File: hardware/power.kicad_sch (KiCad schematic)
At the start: 8 parts, among them U4 MD57E33QA3, U5 MD57E33QA3, U7 TP4054

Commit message: battery switching
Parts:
- added C28: 1uF, Capacitor_SMD:C_0805_2012Metric_Pad1.18x1.45mm_HandSolder, symbol Device:C
- added D1: 1N5819WS, Diode_SMD:D_SOD-323, symbol Diode:1N5819WS
- added D2: LED, symbol Device:LED
- added Q1: AO3401A, Package_TO_SOT_SMD:SOT-23, symbol Transistor_FET:AO3401A
- added R7: 100k, Resistor_SMD:R_0805_2012Metric_Pad1.20x1.40mm_HandSolder, symbol Device:R
- added R8, R9: 2k, Resistor_SMD:R_0805_2012Metric_Pad1.20x1.40mm_HandSolder, symbol Device:R
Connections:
- net +5V: now also C28.1, D1.1 (K), Q1.3 (D)
- net +BATT: now also Q1.2 (S)
- net GND: now also C28.2, R7.2, R8.2
- net VBUS: now also D1.2 (A), Q1.1 (G), R7.1, R9.1
- net at U7.1 (~{CHRG}): now also D2.1 (K)
- net at U7.5 (PROG): now also R8.1
- new net: D2.2 (A), R9.2

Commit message: layout + some routing
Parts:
- added J4: JST PH S2B, Connector_JST:JST_PH_S2B-PH-SM4-TB_1x02-1MP_P2.00mm_Horizontal, symbol Connector_Generic_MountingPin:Conn_01x02_MountingPin
- added SW8: SW_SPDT, Button_Switch_SMD:SW_SPDT_PCM12, symbol Switch:SW_SPDT
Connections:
- net +5V: now also SW8.2 (B); no longer C28.1, D1.1 (K), Q1.3 (D)
- net +BATT: now also J4.1 (Pin_1)
- net GND: now also J4.2 (Pin_2)
- new net: C28.1, D1.1 (K), Q1.3 (D), SW8.3 (C)

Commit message: feat: routing
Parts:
- D2: footprint (none) -> LED_SMD:LED_0805_2012Metric
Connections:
- net at C28.1, D1.1 (K), Q1.3 (D): now also SW8.1 (A); no longer SW8.3 (C)
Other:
- moved on the sheet: SW8
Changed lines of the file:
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@@
-	(wire
-		(pts
-			(xy 130.81 118.11) (xy 132.08 118.11)
-		)
-		(stroke
-			(width 0)
-			(type default)
-		)
-	)
 	(wire
 		(pts
@@
 	(wire
 		(pts
-			(xy 130.81 109.22) (xy 130.81 118.11)
-		)
-		(stroke
-			(width 0)
-			(type default)
-		)
-	)
-	(wire
-		(pts
 			(xy 160.02 36.83) (xy 160.02 39.37)
 		)
@@
 	(wire
 		(pts
-			(xy 132.08 118.11) (xy 132.08 125.73)
+			(xy 130.81 109.22) (xy 130.81 130.81)
 		)
 		(stroke
@@
 		(pts
 			(xy 57.15 54.61) (xy 67.31 54.61)
+		)
+		(stroke
+			(width 0)
+			(type default)
+		)
+	)
+	(wire
+		(pts
+			(xy 130.81 130.81) (xy 132.08 130.81)
 		)
 		(stroke
@@
 			)
 		)
-		(property "Footprint" ""
+		(property "Footprint" "LED_SMD:LED_0805_2012Metric"
 			(at 132.08 40.64 0)
 			(effects
@@
 	(symbol
 		(lib_id "Switch:SW_SPDT")
-		(at 137.16 125.73 0)
+		(at 137.16 130.81 0)
 		(unit 1)
 		(exclude_from_sim no)
@@
 		(fields_autoplaced yes)
 		(property "Reference" "SW8"
-			(at 137.16 117.9025 0)
+			(at 137.16 122.9825 0)
 			(effects
 				(font
@@
 		)
 		(property "Value" "SW_SPDT"
-			(at 137.16 120.3268 0)
+			(at 137.16 125.4068 0)
 			(effects
 				(font
@@
 		)
 		(property "Footprint" "Button_Switch_SMD:SW_SPDT_PCM12"
-			(at 137.16 125.73 0)
+			(at 137.16 130.81 0)
 			(effects
 				(font
@@
 		)
 		(property "Datasheet" "~"
-			(at 137.16 133.35 0)
+			(at 137.16 138.43 0)
 			(effects
 				(font
@@
 		)
 		(property "Description" "Switch, single pole double throw"
-			(at 137.16 125.73 0)
-			(effects
-				(font
+			(at 137.16 130.81 0)
+			(effects
+				(font

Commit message: feat: hfsdr rough
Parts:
- removed SW8: SW_SPDT, Button_Switch_SMD:SW_SPDT_PCM12, symbol Switch:SW_SPDT
- added SW3: MST-22D18G4-WT, easyeda2kicad:SW-SMD_MST-22D18G4-WT, symbol easyeda2kicad:MST-22D18G4-WT
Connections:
- net +5V: now also SW3.2
- net at C28.1, D1.1 (K), Q1.3 (D): now also SW3.3
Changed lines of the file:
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@@
-	(wire
-		(pts
-			(xy 142.24 128.27) (xy 162.56 128.27)
-		)
-		(stroke
-			(width 0)
-			(type default)
-		)
-	)
 	(wire
 		(pts
@@
 	(wire
 		(pts
+			(xy 135.89 130.81) (xy 135.89 128.27)
+		)
+		(stroke
+			(width 0)
+			(type default)
+		)
+	)
+	(wire
+		(pts
 			(xy 181.61 57.15) (xy 160.02 57.15)
 		)
@@
 	(wire
 		(pts
+			(xy 135.89 128.27) (xy 162.56 128.27)
+		)
+		(stroke
+			(width 0)
+			(type default)
+		)
+	)
+	(wire
+		(pts
 			(xy 181.61 54.61) (xy 181.61 57.15)
 		)
@@
 		(pts
 			(xy 57.15 54.61) (xy 67.31 54.61)
-		)
-		(stroke
-			(width 0)
-			(type default)
-		)
-	)
-	(wire
-		(pts
-			(xy 130.81 130.81) (xy 132.08 130.81)
 		)
 		(stroke
@@
 	)
 	(symbol
-		(lib_id "Switch:SW_SPDT")
-		(at 137.16 130.81 0)
-		(unit 1)
-		(exclude_from_sim no)
-		(in_bom yes)
-		(on_board yes)
-		(dnp no)
-		(fields_autoplaced yes)
-		(property "Reference" "SW8"
-			(at 137.16 122.9825 0)
-			(effects
-				(font
-					(size 1.27 1.27)
-				)
-			)
-		)
-		(property "Value" "SW_SPDT"
-			(at 137.16 125.4068 0)
-			(effects
-				(font
-					(size 1.27 1.27)
-				)
-			)
-		)
-		(property "Footprint" "Button_Switch_SMD:SW_SPDT_PCM12"
-			(at 137.16 130.81 0)
-			(effects
-				(font
-					(size 1.27 1.27)
-				)
-				(hide yes)
-			)
-		)
-		(property "Datasheet" "~"
-			(at 137.16 138.43 0)
-			(effects
-				(font
-					(size 1.27 1.27)
-				)
-				(hide yes)
-			)
-		)
-		(property "Description" "Switch, single pole double throw"
-			(at 137.16 130.81 0)
-			(effects
-				(font
-					(size 1.27 1.27)
-				)
-				(hide yes)
-			)
-		)
-		(pin "2"
-		)
-		(pin "1"
-		)
-		(pin "3"
-		)
-		(instances
-			(project "hfsdr"
-				(path "/a11445ed-c3bd-4d1c-a039-1c09b0dceab8/34aaad8d-c78a-4b16-bc41-13b9a7defd8e"
-					(reference "SW8")
-					(unit 1)
-				)
-			)
-		)
-	)
-	(symbol
 		(lib_id "Connector_Generic_MountingPin:Conn_01x02_MountingPin")
 		(at 207.01 120.65 0)
@@
 					(unit 1)
 				)
+			)
+		)
+	)
+	(symbol
+		(lib_id "easyeda2kicad:MST-22D18G4-WT")
+		(at 130.81 135.89 0)
+		(mirror x)
+		(unit 1)
+		(exclude_from_sim no)
+		(in_bom yes)
+		(on_board yes)
+		(dnp no)
+		(property "Reference" "SW3"
+			(at 123.19 135.8899 0)
+			(effects
+				(font
+					(size 1.27 1.27)
+				)
+				(justify right)
+			)
+		)
+		(property "Value" "MST-22D18G4-WT"
+			(at 123.19 138.4299 0)
+			(effects
+				(font
+					(size 1.27 1.27)
+				)
+				(justify right)
+			)
+		)
+		(property "Footprint" "easyeda2kicad:SW-SMD_MST-22D18G4-WT"
+			(at 130.81 123.19 0)
+			(effects
+				(font
+					(size 1.27 1.27)
+				)
+				(hide yes)
+			)
+		)
+		(property "Datasheet" ""
+			(at 130.81 135.89 0)
+			(effects
+				(font
+					(size 1.27 1.27)
+				)
+				(hide yes)
+			)
+		)
+		(property "Description" ""
+			(at 130.81 135.89 0)
+			(effects
+				(font
+					(size 1.27 1.27)
+				)
+				(hide yes)
+			)
+		)
+		(property "LCSC Part" "C7507448"
+			(at 130.81 120.65 0)
+			(effects
+				(font
+					(size 1.27 1.27)
+				)
+				(hide yes)
+			)
+		)
+		(pin "1"
+		)
+		(pin "6"
+		)
+		(pin "4"
+		)
+		(pin "3"
+		)
+		(pin "2"
+		)
+		(pin "5"
+		)
+		(instances
+			(project ""
+				(path "/a11445ed-c3bd-4d1c-a039-1c09b0dceab8/34aaad8d-c78a-4b16-bc41-13b9a7defd8e"
+					(reference "SW3")
+					(unit 1)
+				)

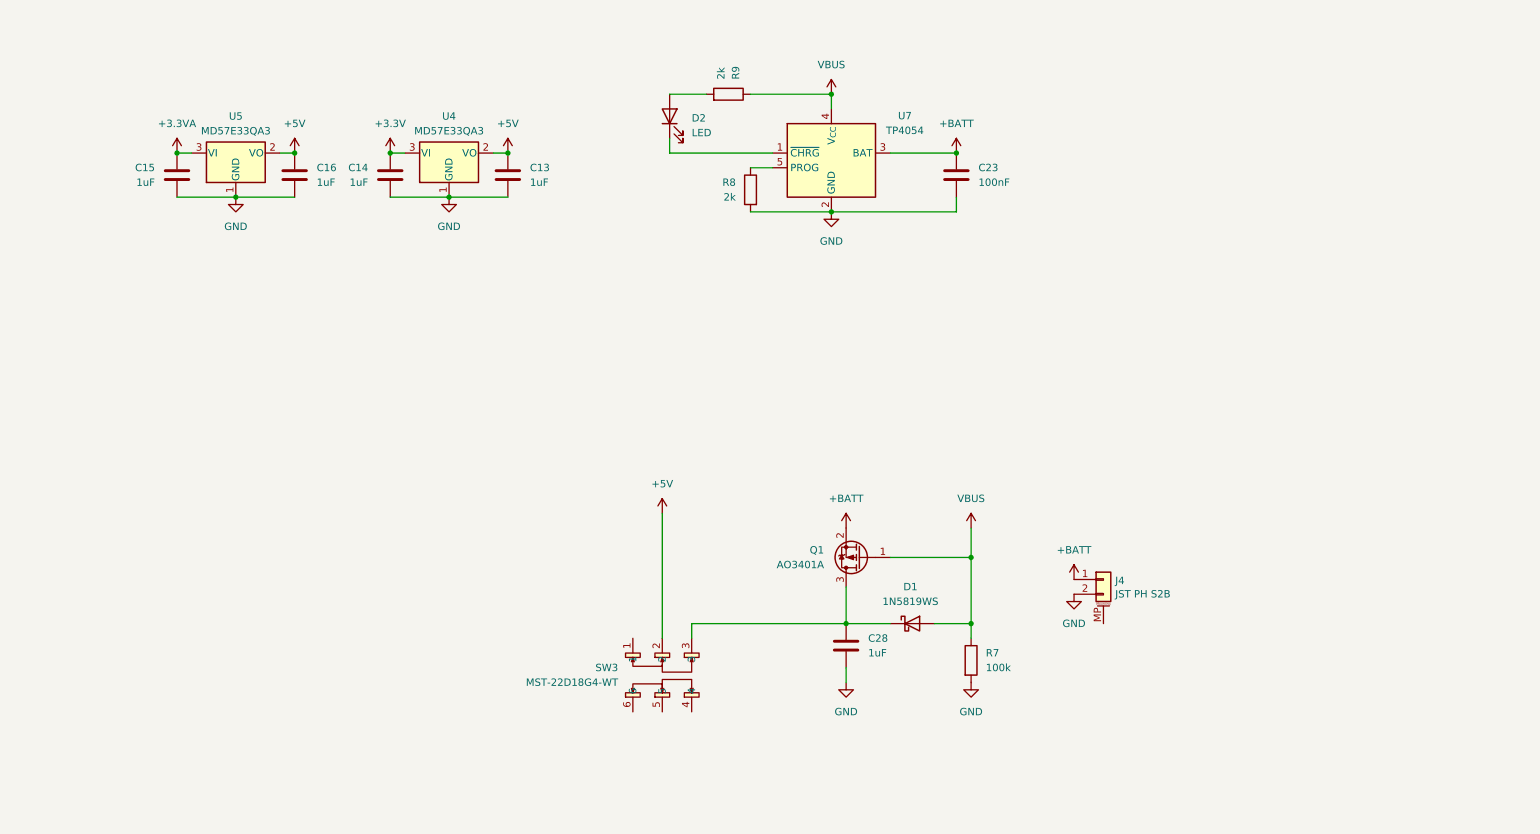
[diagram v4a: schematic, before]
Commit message: feat: add pads + fix adc chip footprint
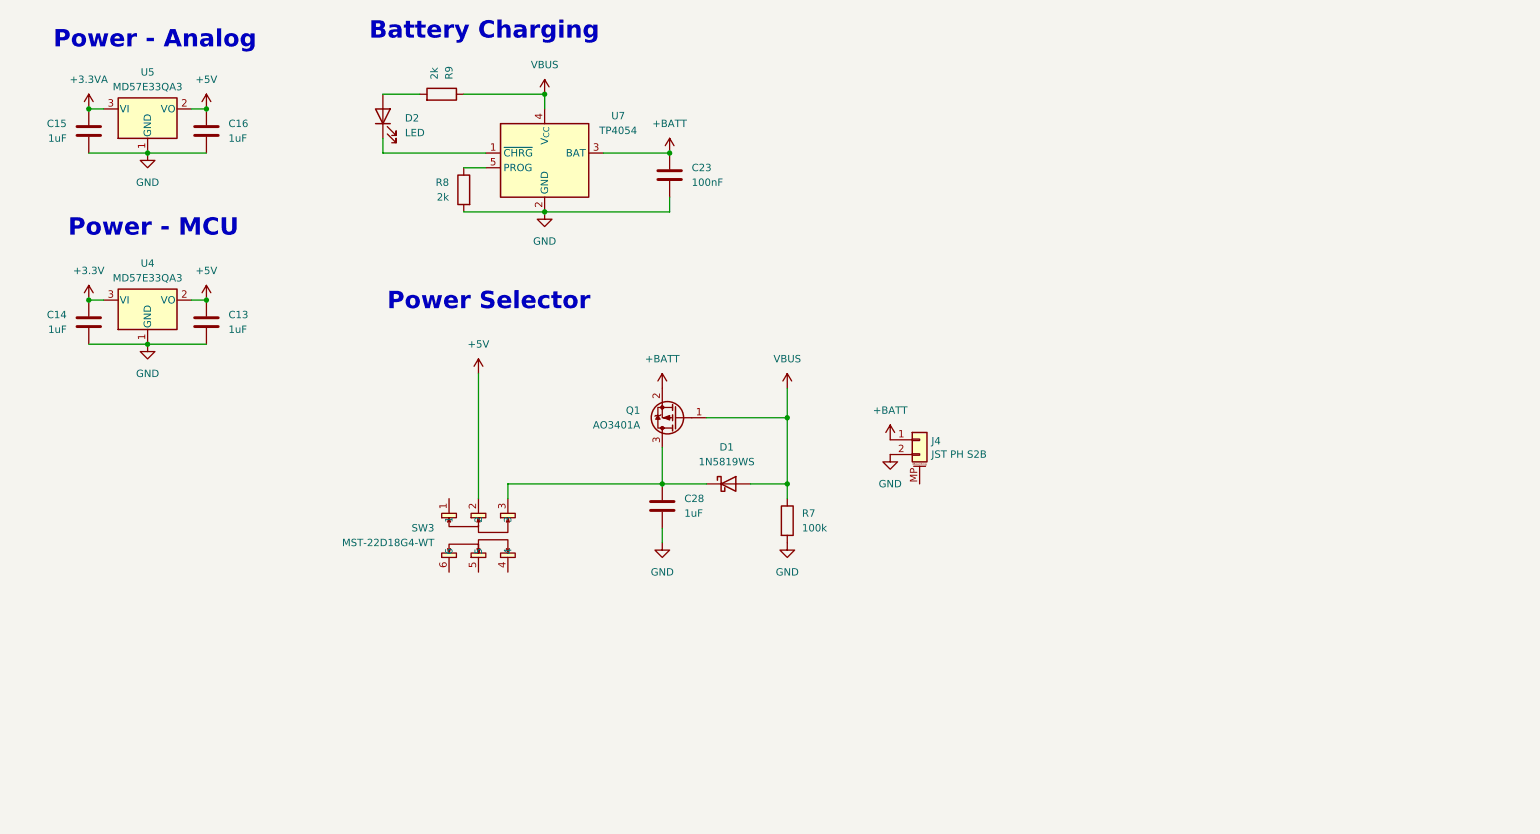
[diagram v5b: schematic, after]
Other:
- note added: "Battery Charging"
- note added: "Power - Analog"
- note added: "Power - MCU"
- note added: "Power Selector"
- moved on the sheet: C13, C14, C15, C16, C23, C28, D1, D2, J4, Q1, R7, R8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

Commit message: Production ready
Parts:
- removed U4, U5: MD57E33QA3, Package_TO_SOT_SMD:SOT-23, symbol Regulator_Linear:TPS7A0520PDBZ
- added R19, R20, R21, R22: 220k, Resistor_SMD:R_0805_2012Metric_Pad1.20x1.40mm_HandSolder, symbol Device:R
- added U10, U9: LMV321, Package_TO_SOT_SMD:SOT-353_SC-70-5, symbol Amplifier_Operational:LMV321
- added U4, U5: MD57E33QC3, easyeda:SOT-23-5_L3.0-W1.7-P0.95-LS2.8-BR, symbol easyeda:MD57E33QC3
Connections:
- net +3.3V: now also U10.5 (V+), U4.5 (VOUT), U9.5 (V+)
- net +3.3VA: now also U5.5 (VOUT)
- net +5V: now also U4.1 (VIN), U4.3 (EN), U5.1 (VIN), U5.3 (EN)
- net +BATT: now also R19.1
- net GND: now also R20.2, R22.2, U10.2 (V-), U4.2 (GND), U5.2 (GND), U9.2 (V-)
- net VBUS: now also R21.1
- new net: R21.2, R22.1, U10.1 (+)
- new net: R19.2, R20.1, U9.1 (+)
- new net BATT_ADC: U9.3 (-), U9.4
- new net VBUS_ADC: U10.3 (-), U10.4
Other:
- moved on the sheet: C13, C14, C15, C16

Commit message: Update hardware
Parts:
- removed U10, U9: LMV321, Package_TO_SOT_SMD:SOT-353_SC-70-5, symbol Amplifier_Operational:LMV321
- added C49, C50: 100nF, Capacitor_SMD:C_0805_2012Metric_Pad1.18x1.45mm_HandSolder, symbol Device:C
- R19, R20, R21, R22: value 220k -> 47k
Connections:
- net +5V: now also SW3.5; no longer SW3.2
- net +BATT: now also SW3.3; no longer R19.1
- net BATT_ADC: now also R19.2, R20.1, C49.1
- net GND: now also C49.2, C50.2
- net VBUS_ADC: now also R21.2, R22.1, C50.1
- net at C28.1, D1.1 (K), Q1.3 (D): now also SW3.4; no longer SW3.3
- new net: R19.1, SW3.2
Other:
- moved on the sheet: R19, R20, R21, R22

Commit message: production
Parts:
- added C55: 100nF, Capacitor_SMD:C_0805_2012Metric_Pad1.18x1.45mm_HandSolder, symbol Device:C
- added C56: 1uF, Capacitor_SMD:C_0805_2012Metric_Pad1.18x1.45mm_HandSolder, symbol Device:C
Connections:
- net +5V: now also C55.2, C56.2
- net GND: now also C55.1, C56.1
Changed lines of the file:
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@@
 	)
 	(junction
+		(at 64.77 31.75)
+		(diameter 0)
+		(color 0 0 0 0)
+	)
+	(junction
 		(at 36.83 55.88)
 		(diameter 0)
@@
 	)
 	(junction
+		(at 64.77 41.91)
+		(diameter 0)
+		(color 0 0 0 0)
+	)
+	(junction
 		(at 59.69 85.09)
 		(diameter 0)
@@
 	)
 	(junction
+		(at 64.77 39.37)
+		(diameter 0)
+		(color 0 0 0 0)
+	)
+	(junction
 		(at 26.67 41.91)
 		(diameter 0)
@@
 	(wire
 		(pts
+			(xy 64.77 31.75) (xy 74.93 31.75)
+		)
+		(stroke
+			(width 0)
+			(type default)
+		)
+	)
+	(wire
+		(pts
 			(xy 142.24 154.94) (xy 152.4 154.94)
 		)
@@
 	(wire
 		(pts
+			(xy 64.77 39.37) (xy 74.93 39.37)
+		)
+		(stroke
+			(width 0)
+			(type default)
+		)
+	)
+	(wire
+		(pts
 			(xy 82.55 46.99) (xy 100.33 46.99)
 		)
@@
 	(wire
 		(pts
+			(xy 64.77 39.37) (xy 64.77 41.91)
+		)
+		(stroke
+			(width 0)
+			(type default)
+		)
+	)
+	(wire
+		(pts
 			(xy 152.4 92.71) (xy 152.4 87.63)
 		)
@@
 	(symbol
 		(lib_id "power:GND")
+		(at 64.77 31.75 180)
+		(unit 1)
+		(exclude_from_sim no)
+		(in_bom yes)
+		(on_board yes)
+		(dnp no)
+		(fields_autoplaced yes)
+		(property "Reference" "#PWR093"
+			(at 64.77 25.4 0)
+			(effects
+				(font
+					(size 1.27 1.27)
+				)
+				(hide yes)
+			)
+		)
+		(property "Value" "GND"
+			(at 64.77 26.67 0)
+			(effects
+				(font
+					(size 1.27 1.27)
+				)
+			)
+		)
+		(property "Footprint" ""
+			(at 64.77 31.75 0)
+			(effects
+				(font
+					(size 1.27 1.27)
+				)
+				(hide yes)
+			)
+		)
+		(property "Datasheet" ""
+			(at 64.77 31.75 0)
+			(effects
+				(font
+					(size 1.27 1.27)
+				)
+				(hide yes)
+			)
+		)
+		(property "Description" "Power symbol creates a global label with name \"GND\" , ground"
+			(at 64.77 31.75 0)
+			(effects
+				(font
+					(size 1.27 1.27)
+				)
+				(hide yes)
+			)
+		)
+		(pin "1"
+		)
+		(instances
+			(project "hfsdr"
+				(path "/a11445ed-c3bd-4d1c-a039-1c09b0dceab8/34aaad8d-c78a-4b16-bc41-13b9a7defd8e"
+					(reference "#PWR093")
+					(unit 1)
+				)
+			)
+		)
+	)
+	(symbol
+		(lib_id "power:GND")
 		(at 53.34 44.45 90)
 		(mirror x)
@@
 	)
 	(symbol
+		(lib_id "Device:C")
+		(at 64.77 35.56 0)
+		(unit 1)
+		(exclude_from_sim no)
+		(in_bom yes)
+		(on_board yes)
+		(dnp no)
+		(property "Reference" "C55"
+			(at 67.31 34.036 0)
+			(effects
+				(font
+					(size 1.27 1.27)
+				)
+				(justify left)
+			)
+		)
+		(property "Value" "100nF"
+			(at 66.802 37.338 0)
+			(effects
+				(font
+					(size 1.27 1.27)
+				)
+				(justify left)
+			)
+		)
+		(property "Footprint" "Capacitor_SMD:C_0805_2012Metric_Pad1.18x1.45mm_HandSolder"
+			(at 65.7352 39.37 0)
+			(effects
+				(font
+					(size 1.27 1.27)
+				)
+				(hide yes)
+			)
+		)
+		(property "Datasheet" "~"
+			(at 64.77 35.56 0)
+			(effects
+				(font
+					(size 1.27 1.27)
+				)
+				(hide yes)
+			)
+		)
+		(property "Description" "Unpolarized capacitor"
+			(at 64.77 35.56 0)
+			(effects
+				(font
+					(size 1.27 1.27)
+				)
+				(hide yes)
+			)
+		)
+		(pin "2"
+		)
+		(pin "1"
+		)
+		(instances
+			(project "hfsdr"
+				(path "/a11445ed-c3bd-4d1c-a039-1c09b0dceab8/34aaad8d-c78a-4b16-bc41-13b9a7defd8e"
+					(reference "C55")
+					(unit 1)
+				)
+			)
+		)
+	)
+	(symbol
 		(lib_id "power:+5V")
 		(at 54.61 41.91 0)
@@
 					(unit 1)
 				)
+			)
+		)
+	)
+	(symbol
+		(lib_id "Device:C")
+		(at 74.93 35.56 0)
+		(unit 1)
+		(exclude_from_sim no)
+		(in_bom yes)
+		(on_board yes)
+		(dnp no)
+		(fields_autoplaced yes)
+		(property "Reference" "C56"
+			(at 78.74 34.2899 0)
+			(effects
+				(font
+					(size 1.27 1.27)
+				)
+				(justify left)
+			)
+		)
+		(property "Value" "1uF"
+			(at 78.74 36.8299 0)
+			(effects
+				(font
+					(size 1.27 1.27)
+				)
+				(justify left)
+			)
+		)
+		(property "Footprint" "Capacitor_SMD:C_0805_2012Metric_Pad1.18x1.45mm_HandSolder"
+			(at 75.8952 39.37 0)
+			(effects
+				(font
+					(size 1.27 1.27)
+				)
+				(hide yes)
+			)
+		)
+		(property "Datasheet" "~"
+			(at 74.93 35.56 0)
+			(effects
+				(font
+					(size 1.27 1.27)
+				)
+				(hide yes)
+			)
+		)
+		(property "Description" "Unpolarized capacitor"
+			(at 74.93 35.56 0)
+			(effects
+				(font
+					(size 1.27 1.27)
+				)
+				(hide yes)
+			)
+		)
+		(pin "2"
+		)
+		(pin "1"
+		)
+		(instances
+			(project "hfsdr"
+				(path "/a11445ed-c3bd-4d1c-a039-1c09b0dceab8/34aaad8d-c78a-4b16-bc41-13b9a7defd8e"
+					(reference "C56")
+					(unit 1)
+				)
